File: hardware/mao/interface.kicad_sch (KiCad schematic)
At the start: 24 parts, among them J301 LCD, Q302 DMG2302UKQ, SW301 SKQGADE010, U301 DRV5012AEDMRR, U302 DRV5012AEDMRR, U304 TLV9061IDBVR

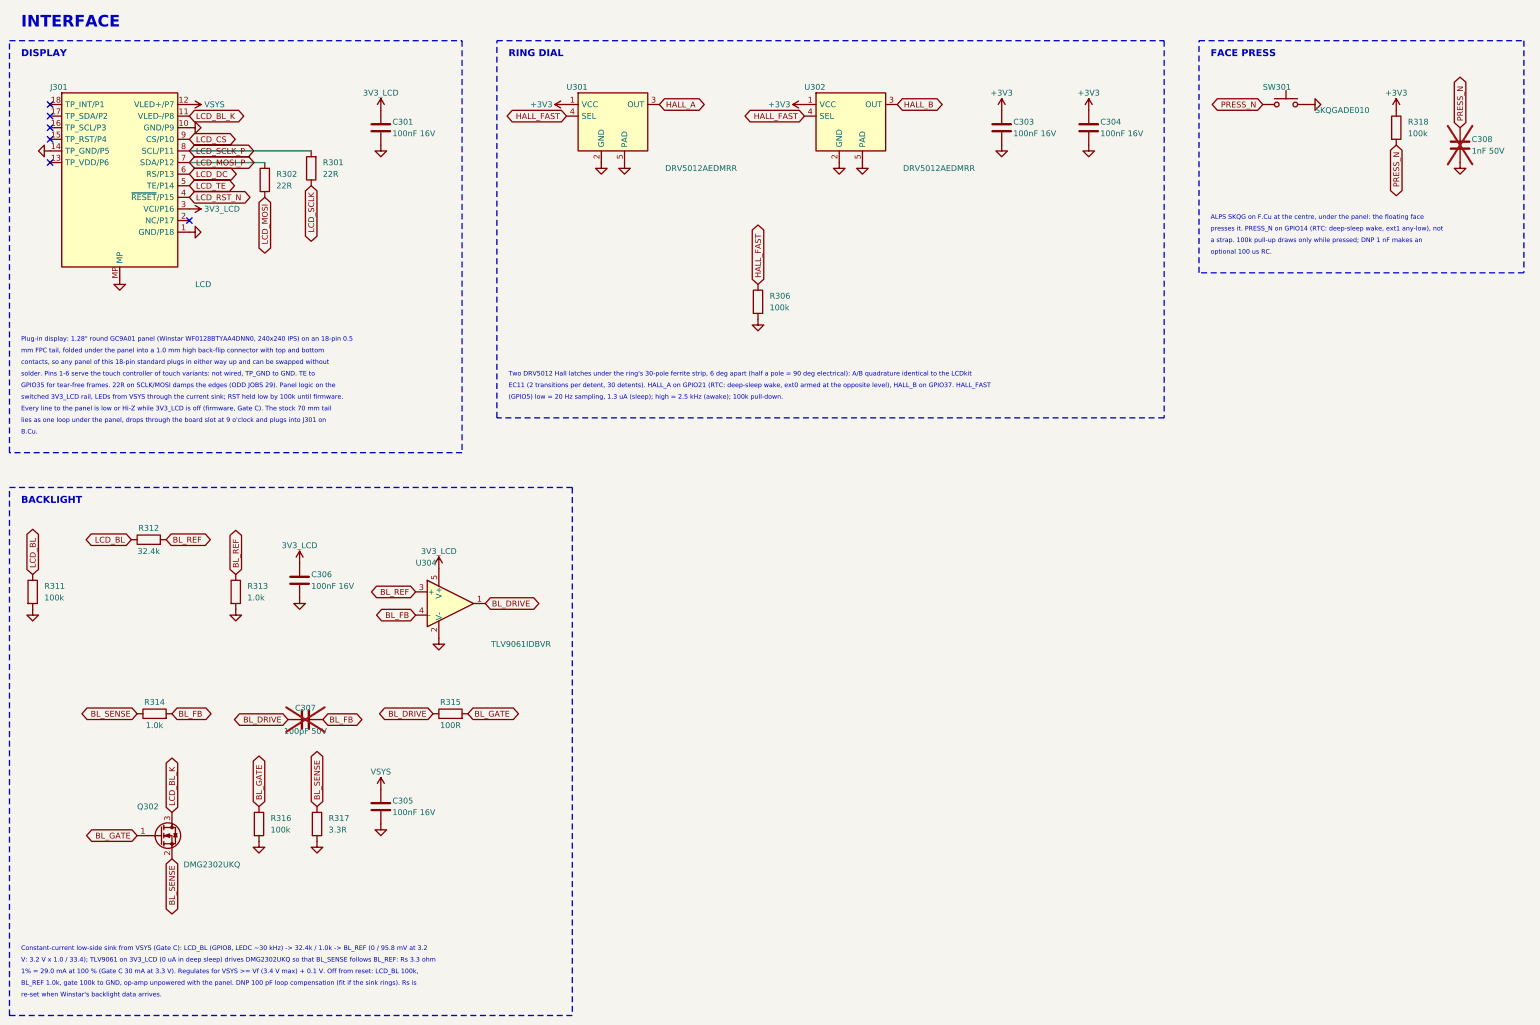
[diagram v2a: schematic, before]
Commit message: A1 face press: tripod of three ALPS SKQGAFE010 (owner decision 2026-10-06)
Three 0.98 N / 0.25 mm / 1.5 mm SKQG switches (C202424) in parallel on PRESS_N
at 70 / 190 / 310 deg (r 17.6 / 14.5 / 14.5) replace the single SKQGADE010 at
the centre; no pin or firmware change. The 3 o'clock half of the panel area is
the tail well, the IR receiver and the charger, so the 70 deg switch takes the
only pocket there at r 17.6. Surgical: sync_fields --add, route_tripod.py
place / rip / add (I2C pair through SW301's channel, PRESS_N to each switch,
IMU_INT1 / AMP_BCLK / HALL_FAST round SW302, GND vias); SKQG legs jumpered
inside the part (build_pcb.JUMPERED_LEGS). Maker mark and S/N field find a
clear spot under the panel. DRC 0/0/0, planes one piece, mech 0 findings.

Co-Authored-By: Claude Opus 5.5 <noreply@anthropic.com>
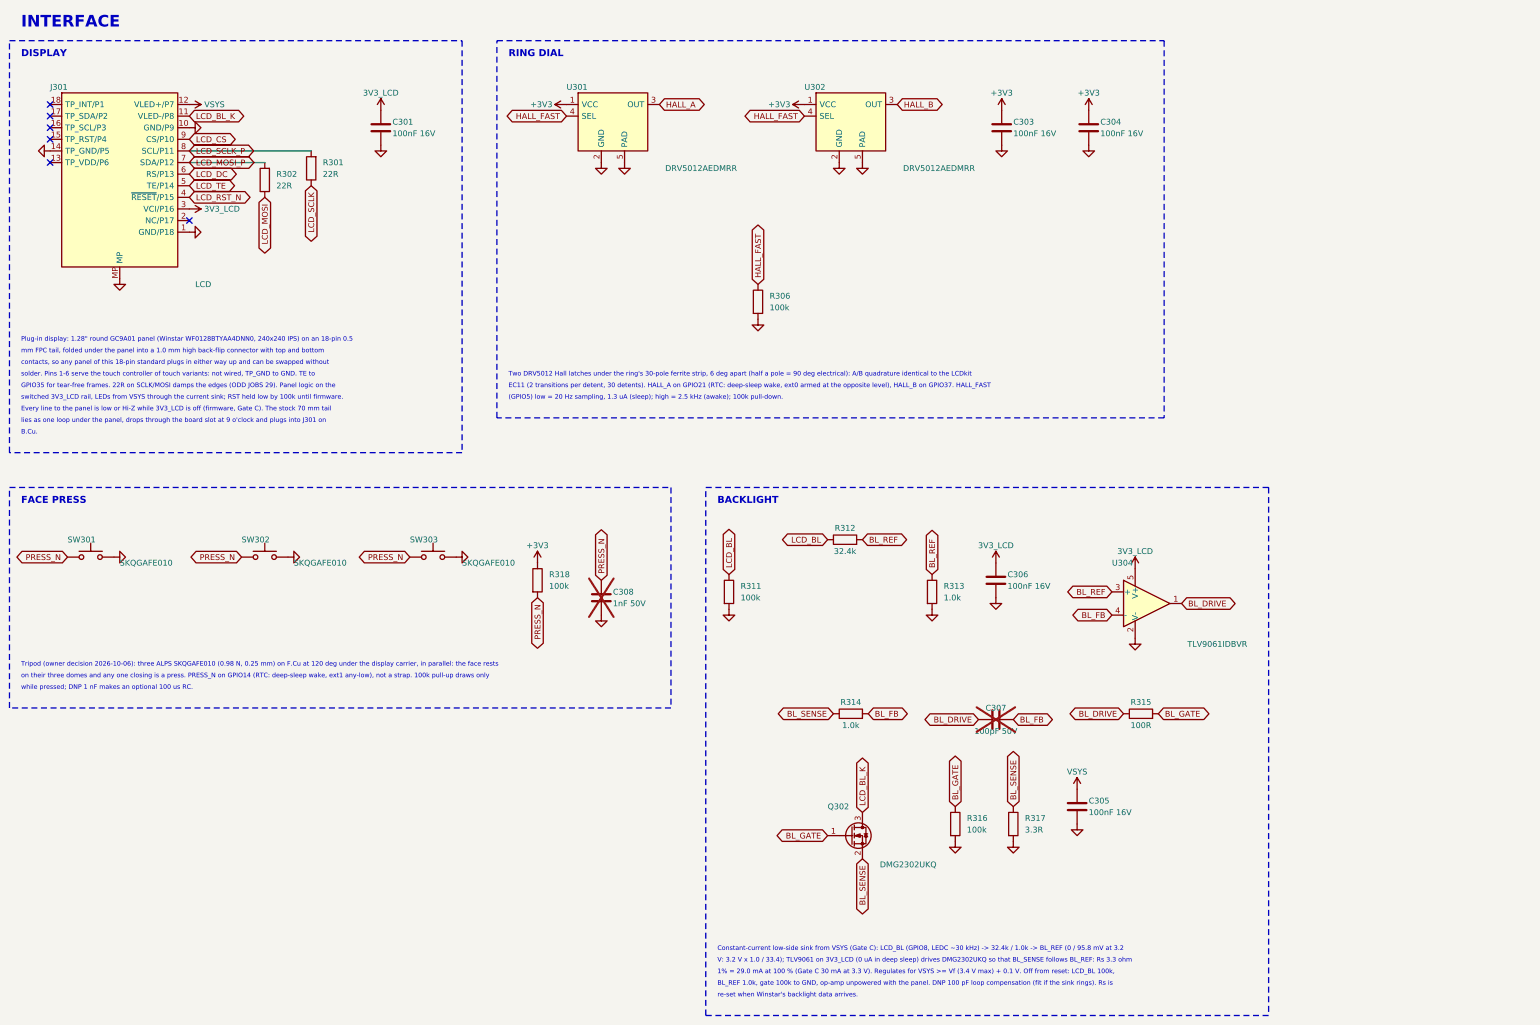
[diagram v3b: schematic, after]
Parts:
- added SW302, SW303: SKQGAFE010, Button_Switch_SMD:SW_SPST_SKQG_WithStem, symbol Switch:SW_Push
- SW301: value SKQGADE010 -> SKQGAFE010; LCSC C116647 -> C202424; MPN SKQGADE010 -> SKQGAFE010
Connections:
- net GND: now also SW302.2, SW303.2
- net PRESS_N: now also SW302.1, SW303.1
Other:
- note added: "Tripod (owner decision 2026-10-06): three ALPS SKQGAFE010 (0.98 N, 0.25 mm) on F.Cu at 120 deg under the display carrier, in parallel: the face rests"
- note added: "on their three domes and any one closing is a press. PRESS_N on GPIO14 (RTC: deep-sleep wake, ext1 any-low), not a strap. 100k pull-up draws only"
- note added: "while pressed; DNP 1 nF makes an optional 100 us RC."
- note removed: "ALPS SKQG on F.Cu at the centre, under the panel: the floating face"
- note removed: "a strap. 100k pull-up draws only while pressed; DNP 1 nF makes an"
- note removed: "optional 100 us RC."
- note removed: "presses it. PRESS_N on GPIO14 (RTC: deep-sleep wake, ext1 any-low), not"
- moved on the sheet: C305, C306, C307, C308, Q302, R311, R312, R313, R314, R315, R316, R317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

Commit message: A1 press: P3, the whole top presses one switch on the back (owner decision 2026-10-07)
The face tripod (three SKQGAFE010 on F) gives way to P3: wheel, bezel, window,
panel, carrier, frame and the board slide 0.45 mm on the base; one ALPS
SKQGADE010 (C116647) on B.Cu at (8.0, 3.8) meets a 1.5 mm stainless finger
fixed to the base, reaching over the cell from 12 o'clock.

Board: SW302/SW303 removed, SW301 to B, TP19 steps 0.45 mm, the tail well
back to x 6..12; route_press3.py records the place/well/rip/escape/add steps
(CHG_STAT1/2, I2C_SCL, HALL_A and LCD_TE re-drawn by hand after a free-space
search). Silk re-placed (boop on B, S/N field empty inside). ERC 0, DRC 0 /
0 unconnected / 0 parity, planes one piece, mech 0, silk 0, stack-up
broadside 16.8 mm, fab BOM 49 lines / 100 parts.

Enclosure: guide columns with brass spacers in the base (the hard stop),
the frame wall slotted round them, snap ledges and pins for the board, the
finger and its root posts, carrier feet; clash check 0 at rest and pressed.
Finger STL (fit) and DXF (laser cut); sections, renders, plots, docs.

Co-Authored-By: Claude Opus 5.5 <noreply@anthropic.com>
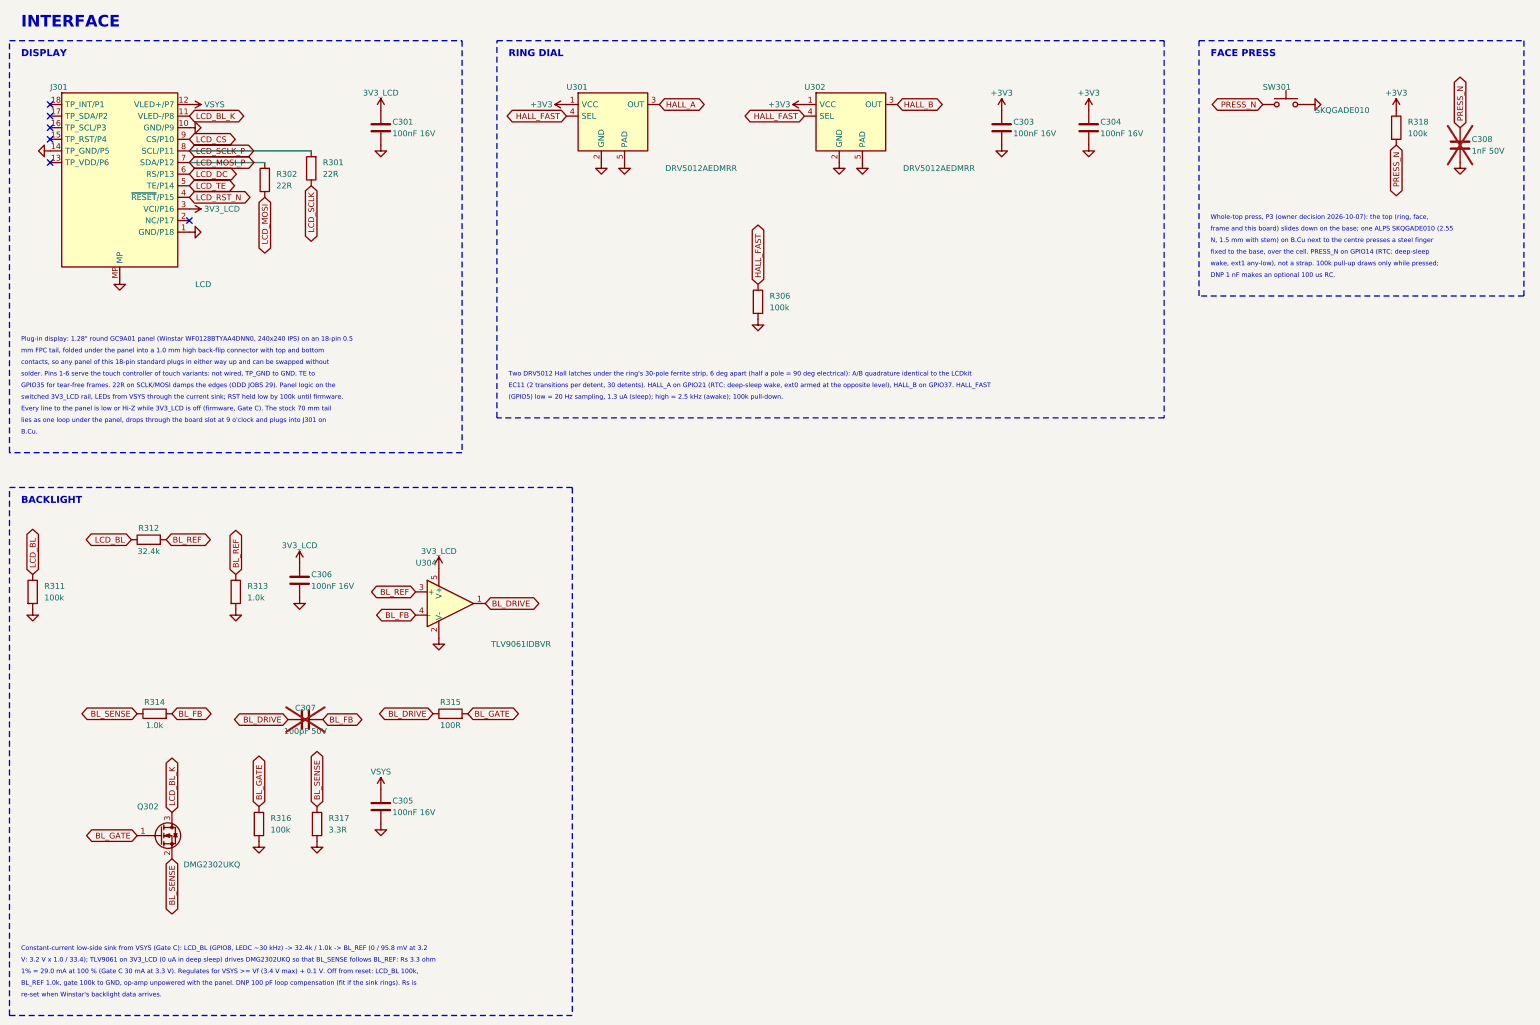
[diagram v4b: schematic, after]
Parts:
- removed SW302, SW303: SKQGAFE010, Button_Switch_SMD:SW_SPST_SKQG_WithStem, symbol Switch:SW_Push
- SW301: value SKQGAFE010 -> SKQGADE010; LCSC C202424 -> C116647; MPN SKQGAFE010 -> SKQGADE010
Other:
- note added: "DNP 1 nF makes an optional 100 us RC."
- note added: "N, 1.5 mm with stem) on B.Cu next to the centre presses a steel finger"
- note added: "Whole-top press, P3 (owner decision 2026-10-07): the top (ring, face,"
- note added: "fixed to the base, over the cell. PRESS_N on GPIO14 (RTC: deep-sleep"
- note added: "frame and this board) slides down on the base; one ALPS SKQGADE010 (2.55"
- note added: "wake, ext1 any-low), not a strap. 100k pull-up draws only while pressed;"
- note removed: "Tripod (owner decision 2026-10-06): three ALPS SKQGAFE010 (0.98 N, 0.25 mm) on F.Cu at 120 deg under the display carrier, in parallel: the face rests"
- note removed: "on their three domes and any one closing is a press. PRESS_N on GPIO14 (RTC: deep-sleep wake, ext1 any-low), not a strap. 100k pull-up draws only"
- note removed: "while pressed; DNP 1 nF makes an optional 100 us RC."
- moved on the sheet: C305, C306, C307, C308, Q302, R311, R312, R313, R314, R315, R316, R317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
